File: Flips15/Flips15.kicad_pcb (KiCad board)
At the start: 2 copper layers, 100 x 100 mm, 68 parts, among them CN1 UFP2810, U1001 74HC238, U1002 ULN2803A, U1003 74HC238, U1004 TBD62783A, U1101 74HC238, U1102 ULN2803A, U1103 74HC238, U1104 TBD62783A, U701 74HC238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

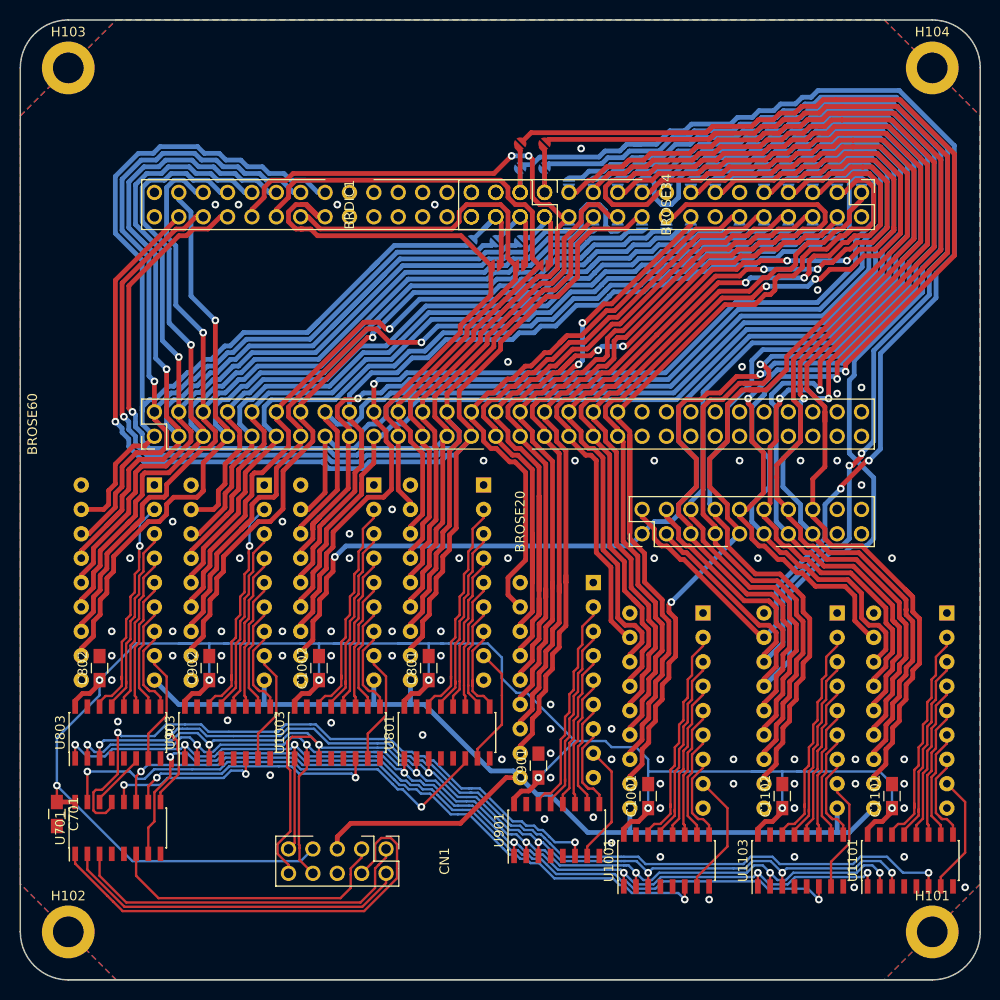
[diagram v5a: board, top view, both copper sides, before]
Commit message: Simplify traces
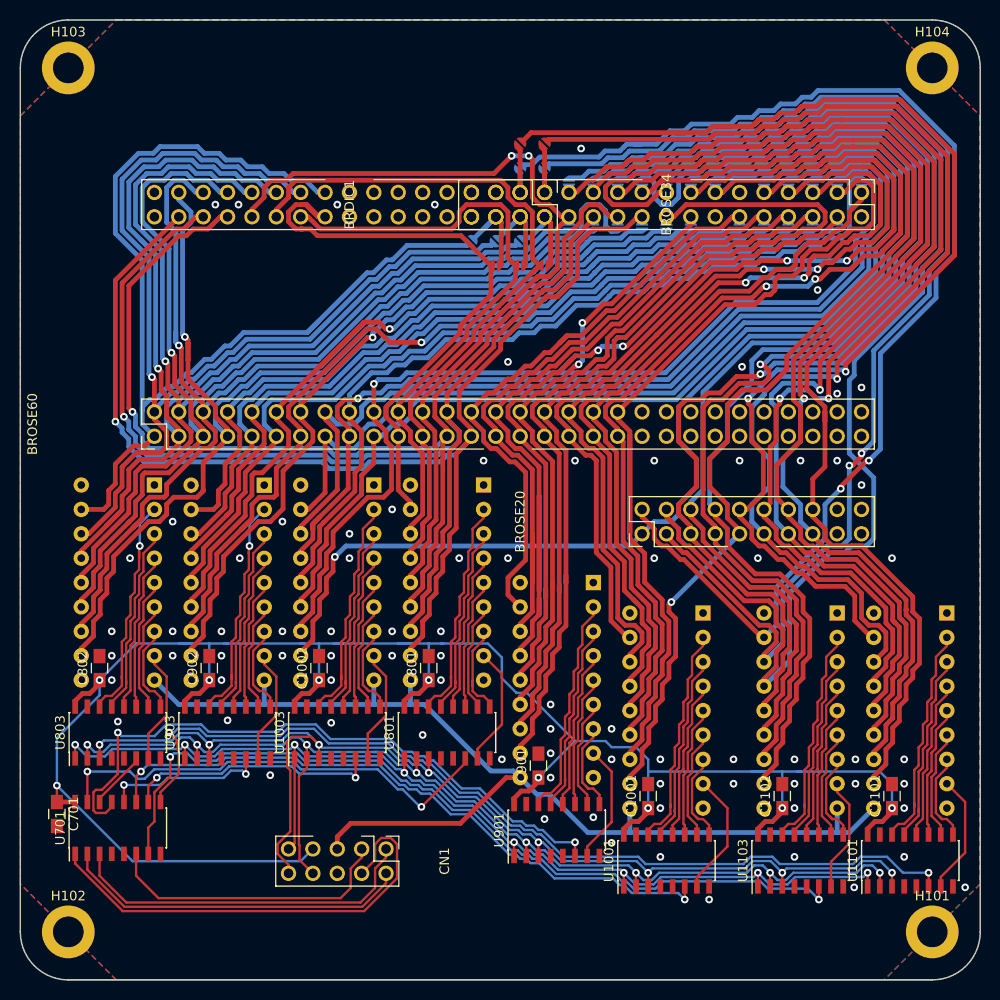
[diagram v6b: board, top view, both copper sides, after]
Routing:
- net /SY3: track 122.5 -> 114.7 mm
- net /SY7: track 114.6 -> 117.0 mm
- net /SY1: track 110.7 -> 109.7 mm
- net /SY6: track 109.3 -> 110.2 mm
- net /UnitY/E3H: track 88.8 -> 88.1 mm
- net /UnitY/Group0/YH1: track 24.9 -> 24.2 mm

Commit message: Fixing alignment of board to 0.025 in grid
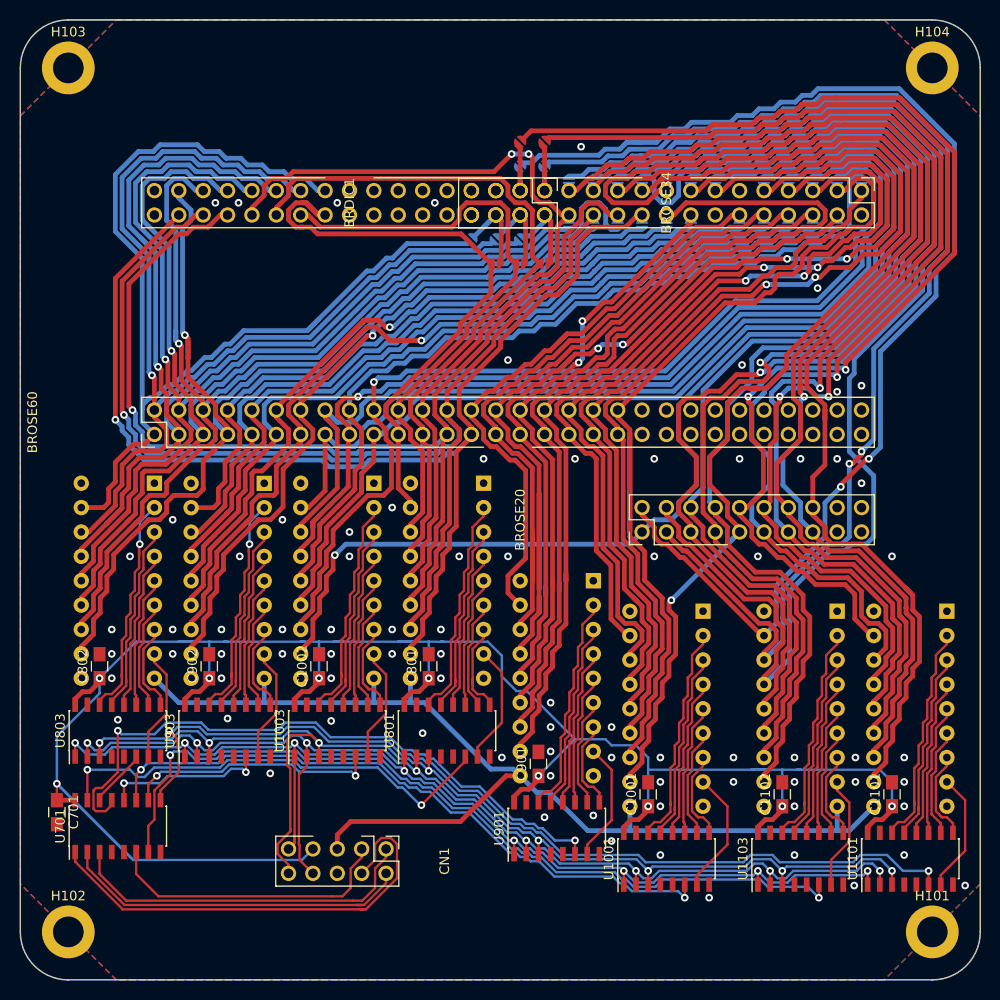
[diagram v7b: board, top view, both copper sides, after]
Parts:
- moved U1001 0.19 mm to (118.1, 138.2)
- moved U1101 0.19 mm to (143.5, 138.2)
- moved U1103 0.19 mm to (132.1, 138.2)
- moved JP115 0.19 mm to (128.3, 67.6)
- moved JP116 0.19 mm to (130.8, 67.6)
- moved JP117 0.19 mm to (133.3, 67.6)
- moved JP118 0.19 mm to (138.4, 67.6)
- moved JP119 0.19 mm to (123.2, 67.6)
- moved JP120 0.19 mm to (135.9, 67.6)
- moved JP121 0.19 mm to (120.7, 67.6)
- moved JP124 0.19 mm to (108.0, 67.6)
- moved JP125 0.19 mm to (110.5, 67.6)
- moved JP126 0.19 mm to (115.6, 67.6)
- moved JP127 0.19 mm to (113.0, 67.6)
- moved JP128 0.19 mm to (118.1, 67.6)
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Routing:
- net VCC: track 208.3 -> 219.4 mm
- net /UnitY/B1: track 37.3 -> 38.1 mm
- net /UnitY/A0: track 113.4 -> 114.1 mm

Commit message: better GND
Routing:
- net GND: track 0.00 -> 49.3 mm, vias 81 -> 79
- net /UnitY/E0H: track 6.12 -> 10.7 mm
- net /UnitY/A2: track 122.5 -> 126.5 mm
- net /UnitY/E0L: track 47.9 -> 50.9 mm
- net /UnitY/E3H: track 88.1 -> 85.3 mm
- net /UnitY/E2H: track 26.6 -> 28.5 mm
- net /UnitY/A1: track 118.6 -> 119.8 mm
- net /UnitY/Group0/YH7: track 12.0 -> 13.0 mm
- net /UnitY/E1H: track 16.9 -> 17.7 mm
- net /UnitY/E3L: track 98.0 -> 97.3 mm
- net /UnitY/E2L: track 69.2 -> 69.7 mm
- net /UnitY/Group3/YH7: track 12.0 -> 12.5 mm
- net /UnitY/Group2/YL7: track 13.1 -> 12.5 mm
- net /UnitY/Group2/YH7: track 12.0 -> 12.5 mm
- net /UnitY/EN: track 30.5 -> 30.0 mm
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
